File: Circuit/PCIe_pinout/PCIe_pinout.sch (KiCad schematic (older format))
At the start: 3 parts

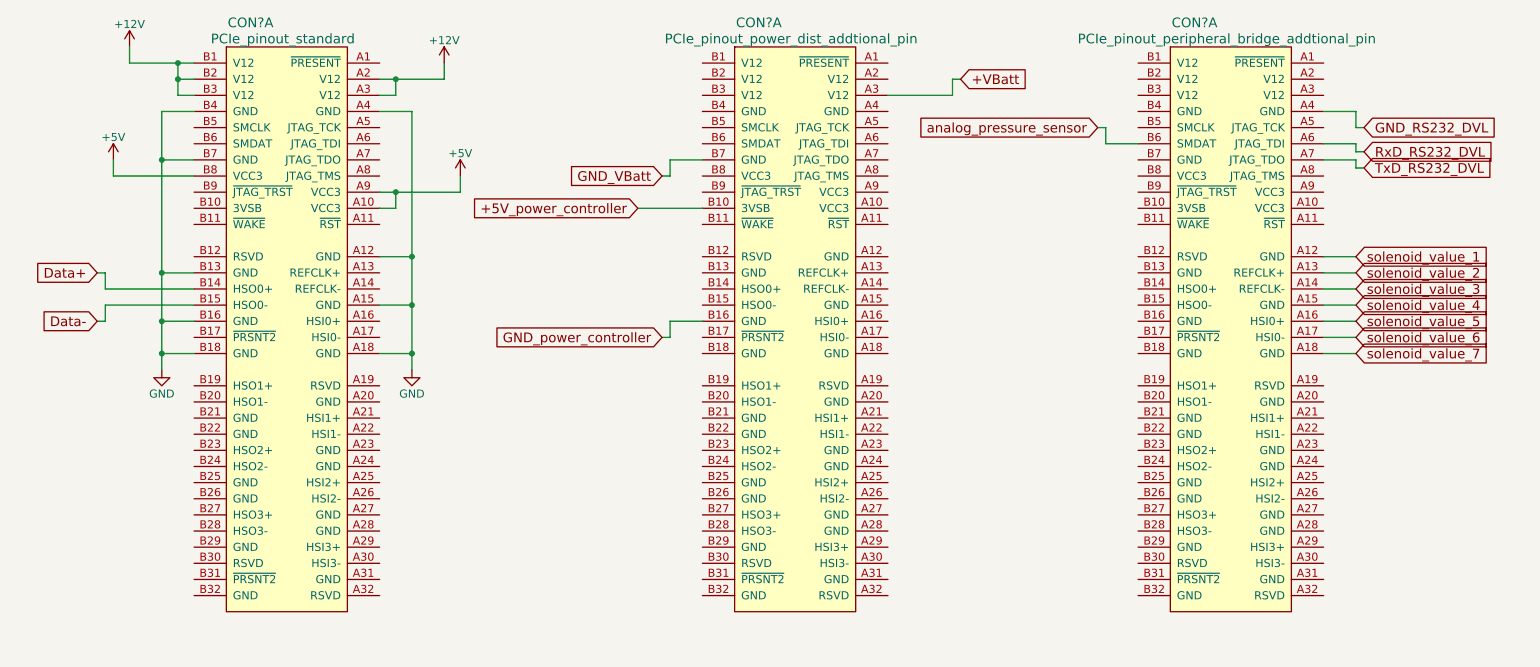
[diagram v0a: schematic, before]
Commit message: add addtional description
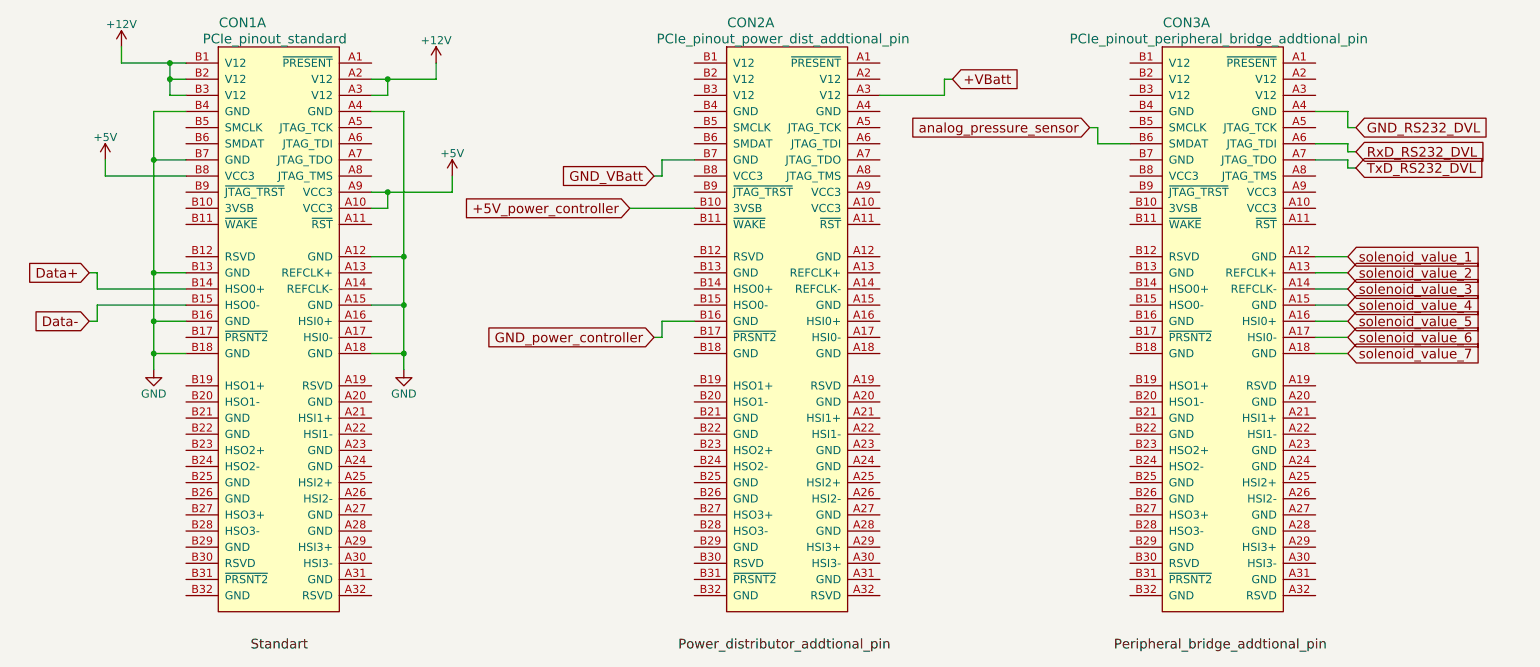
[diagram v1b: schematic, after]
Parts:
- gave numbers to parts that had none: 3
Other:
- moved on the sheet: CON1A, CON2A, CON3A

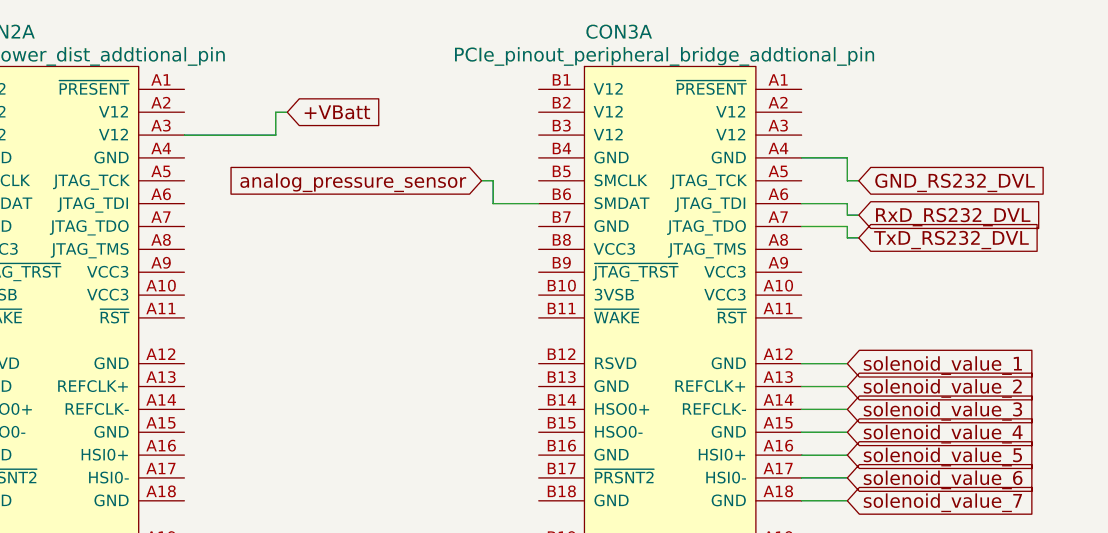
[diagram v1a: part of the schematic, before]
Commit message: added DSP_reset pins to PCIe_pinout
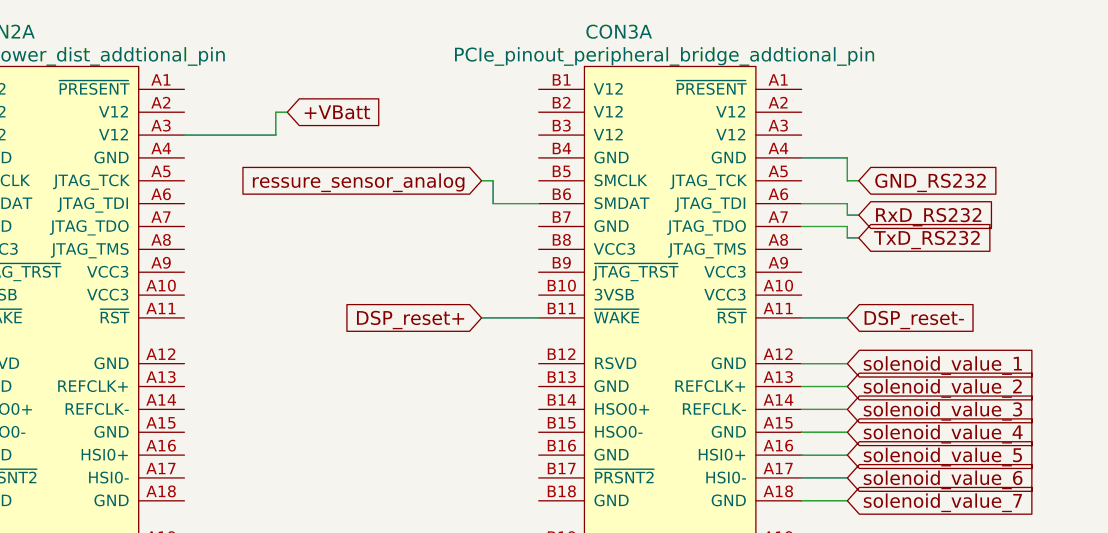
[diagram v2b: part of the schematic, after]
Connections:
- net DSP_reset-: now reaches CON3.A11 (~RST)
- net DSP_reset+: now reaches CON3.B11 (~WAKE)
- net GND_RS232_DVL renamed GND_RS232
- net RxD_RS232_DVL renamed RxD_RS232
- net TxD_RS232_DVL renamed TxD_RS232
- net analog_pressure_sensor renamed ressure_sensor_analog
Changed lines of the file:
@@
 LIBS:valves
 LIBS:zeabus
-LIBS:PCIe_pinout-cache
 EELAYER 25 0
 EELAYER END
@@
 $EndComp
 Text GLabel 7850 2500 0    60   Input ~ 0
-analog_pressure_sensor
+ressure_sensor_analog
 Wire Wire Line
 	7850 2500 7900 2500
@@
 	7900 2600 8100 2600
 Text GLabel 9500 2750 2    60   Input ~ 0
-TxD_RS232_DVL
+TxD_RS232
 Text GLabel 9500 2650 2    60   Input ~ 0
-RxD_RS232_DVL
+RxD_RS232
 Wire Wire Line
 	9250 2600 9450 2600
 Text GLabel 9500 2500 2    60   Input ~ 0
-GND_RS232_DVL
+GND_RS232
 Wire Wire Line
 	9450 2600 9450 2650
@@
 Text Label 8000 5750 0    60   ~ 0
 Peripheral_bridge_addtional_pin
+Text GLabel 7850 3100 0    60   Input ~ 0
+DSP_reset+
+Wire Wire Line
+	7850 3100 8100 3100
+Text GLabel 9450 3100 2    60   Input ~ 0
+DSP_reset-
+Wire Wire Line
+	9450 3100 9250 3100
 $EndSCHEMATC

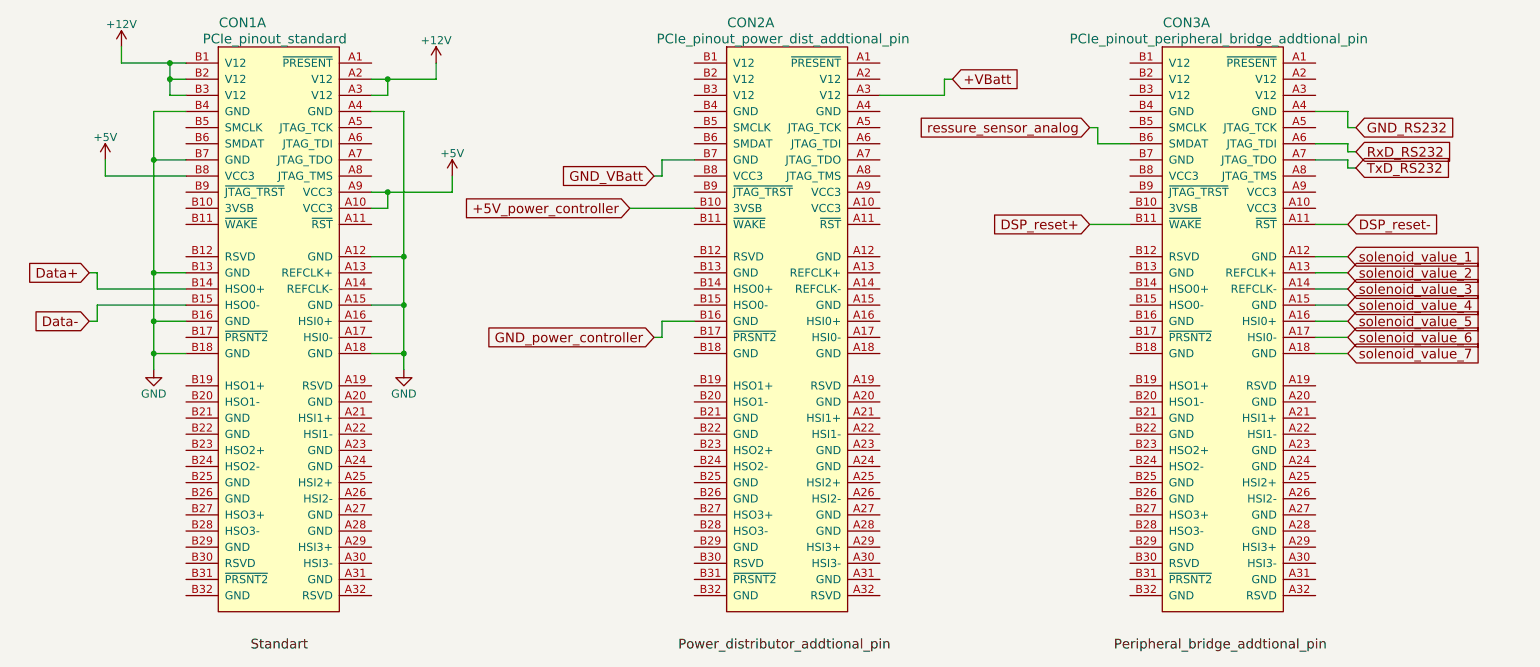
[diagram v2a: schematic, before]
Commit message: added planner_sw to PCIe_pinout
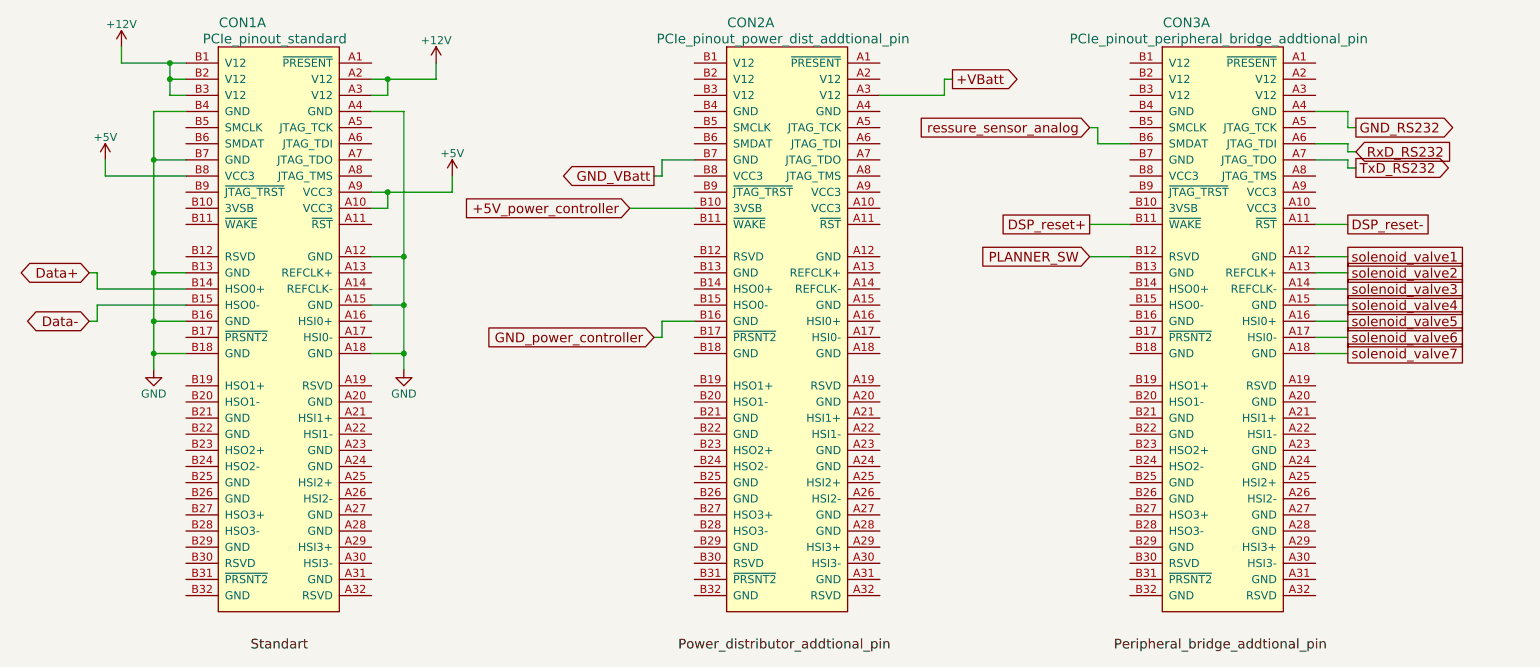
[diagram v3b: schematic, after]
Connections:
- net PLANNER_SW: now reaches CON3.B12 (RSVD)
- net solenoid_value_1 renamed solenoid_valve1
- net solenoid_value_2 renamed solenoid_valve2
- net solenoid_value_3 renamed solenoid_valve3
- net solenoid_value_4 renamed solenoid_valve4
- net solenoid_value_5 renamed solenoid_valve5
- net solenoid_value_6 renamed solenoid_valve6
- net solenoid_value_7 renamed solenoid_valve7
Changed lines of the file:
@@
 LIBS:valves
 LIBS:zeabus
+LIBS:PCIe_pinout-cache
 EELAYER 25 0
 EELAYER END
@@
 	1    0    0    -1
 $EndComp
-Text GLabel 1650 3400 0    60   Input ~ 0
+Text GLabel 1650 3400 0    60   BiDi ~ 0
 Data+
-Text GLabel 1650 3700 0    60   Input ~ 0
+Text GLabel 1650 3700 0    60   BiDi ~ 0
 Data-
 $Comp
@@
 Wire Wire Line
 	1700 3600 2250 3600
-Text GLabel 7000 2200 2    60   Input ~ 0
+Text GLabel 7000 2200 2    60   Output ~ 0
 +VBatt
 Wire Wire Line
 	6950 2200 7000 2200
-Text GLabel 5150 2800 0    60   Input ~ 0
+Text GLabel 5150 2800 0    60   Output ~ 0
 GND_VBatt
 Wire Wire Line
@@
 Wire Wire Line
 	7900 2600 8100 2600
-Text GLabel 9500 2750 2    60   Input ~ 0
+Text GLabel 9500 2750 2    60   Output ~ 0
 TxD_RS232
 Text GLabel 9500 2650 2    60   Input ~ 0
@@
 Wire Wire Line
 	9250 2600 9450 2600
-Text GLabel 9500 2500 2    60   Input ~ 0
+Text GLabel 9500 2500 2    60   Output ~ 0
 GND_RS232
 Wire Wire Line
@@
 Wire Wire Line
 	9450 2400 9250 2400
-Text GLabel 9450 3300 2    60   Input ~ 0
-solenoid_value_1
+Text GLabel 9450 3300 2    60   UnSpc ~ 0
+solenoid_valve1
 Wire Wire Line
 	9250 3300 9450 3300
-Text GLabel 9450 3400 2    60   Input ~ 0
-solenoid_value_2
-Text GLabel 9450 3500 2    60   Input ~ 0
-solenoid_value_3
-Text GLabel 9450 3600 2    60   Input ~ 0
-solenoid_value_4
-Text GLabel 9450 3700 2    60   Input ~ 0
-solenoid_value_5
-Text GLabel 9450 3800 2    60   Input ~ 0
-solenoid_value_6
-Text GLabel 9450 3900 2    60   Input ~ 0
-solenoid_value_7
 Wire Wire Line
 	9450 3900 9250 3900
@@
 Text Label 8000 5750 0    60   ~ 0
 Peripheral_bridge_addtional_pin
-Text GLabel 7850 3100 0    60   Input ~ 0
+Text GLabel 7850 3100 0    60   UnSpc ~ 0
 DSP_reset+
 Wire Wire Line
 	7850 3100 8100 3100
-Text GLabel 9450 3100 2    60   Input ~ 0
+Text GLabel 9450 3100 2    60   UnSpc ~ 0
 DSP_reset-
 Wire Wire Line
 	9450 3100 9250 3100
+Text GLabel 7850 3300 0    60   Input ~ 0
+PLANNER_SW
+Wire Wire Line
+	8100 3300 7850 3300
+Text GLabel 9450 3400 2    60   UnSpc ~ 0
+solenoid_valve2
+Text GLabel 9450 3500 2    60   UnSpc ~ 0
+solenoid_valve3
+Text GLabel 9450 3600 2    60   UnSpc ~ 0
+solenoid_valve4
+Text GLabel 9450 3700 2    60   UnSpc ~ 0
+solenoid_valve5
+Text GLabel 9450 3800 2    60   UnSpc ~ 0
+solenoid_valve6
+Text GLabel 9450 3900 2    60   UnSpc ~ 0
+solenoid_valve7
 $EndSCHEMATC

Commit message: added DSP_reset, planner_sw, kill_sw_pwr, sys_sw_pwr to backplane
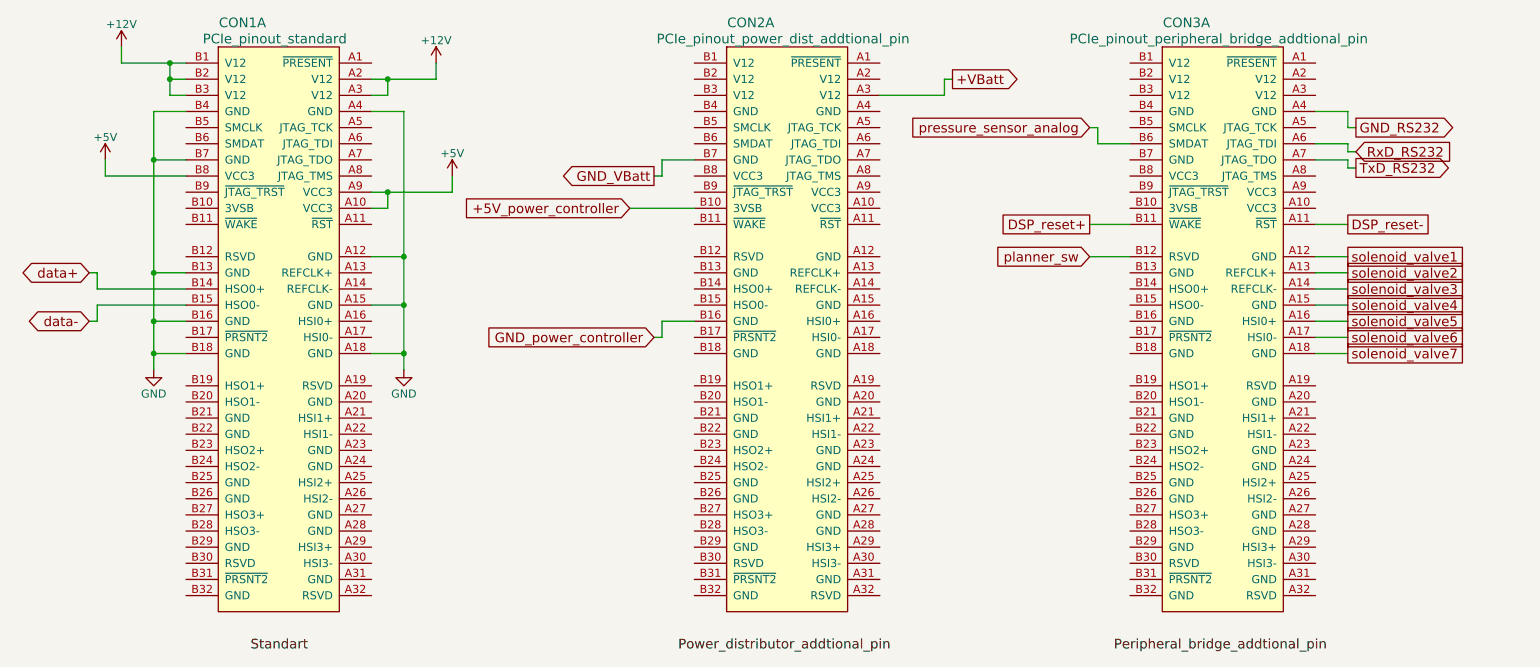
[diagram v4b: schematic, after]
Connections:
- net Data+ renamed data+
- net Data- renamed data-
- net PLANNER_SW renamed planner_sw
- net ressure_sensor_analog renamed pressure_sensor_analog
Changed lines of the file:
@@
 $EndComp
 Text GLabel 1650 3400 0    60   BiDi ~ 0
-Data+
+data+
 Text GLabel 1650 3700 0    60   BiDi ~ 0
-Data-
+data-
 $Comp
 L Conn-PCIE-x16 CON2
@@
 $EndComp
 Text GLabel 7850 2500 0    60   Input ~ 0
-ressure_sensor_analog
+pressure_sensor_analog
 Wire Wire Line
 	7850 2500 7900 2500
@@
 	9450 3100 9250 3100
 Text GLabel 7850 3300 0    60   Input ~ 0
-PLANNER_SW
+planner_sw
 Wire Wire Line
 	8100 3300 7850 3300

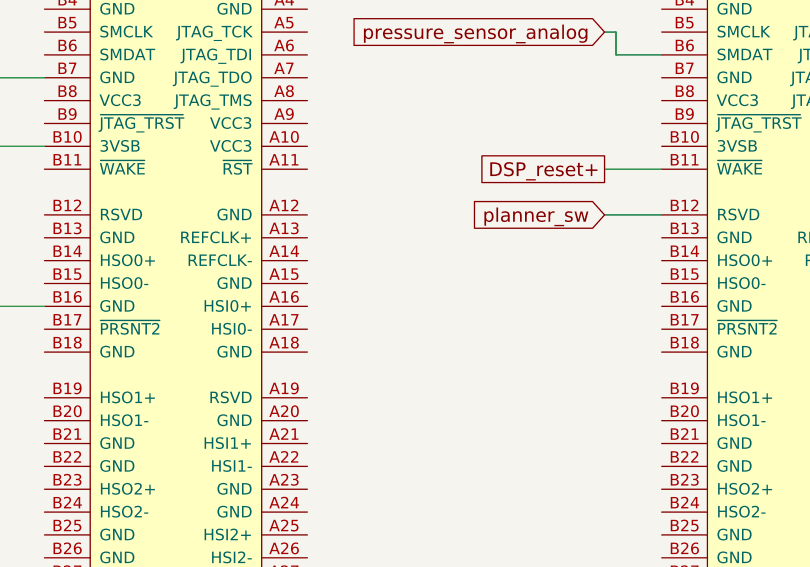
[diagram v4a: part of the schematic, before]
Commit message: added KILL_SW and SYS_SW to power_distributor pinout
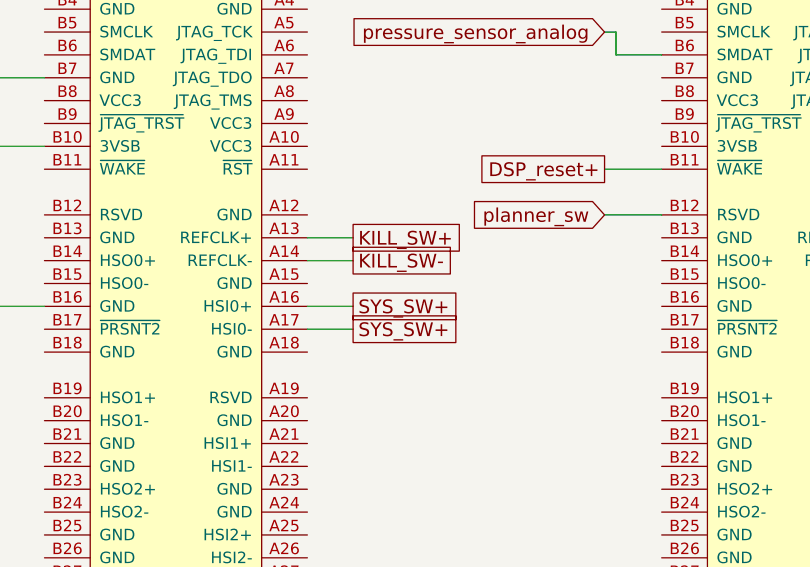
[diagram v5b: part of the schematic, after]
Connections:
- net KILL_SW+: now reaches CON2.A13 (REFCLK+)
- net KILL_SW-: now reaches CON2.A14 (REFCLK-)
- net SYS_SW+: now reaches CON2.A16 (HSI0+)
- net SYS_SW+: now also CON2.A17 (HSI0-)
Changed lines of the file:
@@
 Text GLabel 9450 3900 2    60   UnSpc ~ 0
 solenoid_valve7
+Text GLabel 6750 3400 2    60   UnSpc ~ 0
+KILL_SW+
+Text GLabel 6750 3700 2    60   UnSpc ~ 0
+SYS_SW+
+Text GLabel 6750 3500 2    60   UnSpc ~ 0
+KILL_SW-
+Wire Wire Line
+	6550 3400 6750 3400
+Wire Wire Line
+	6750 3500 6550 3500
+Text GLabel 6750 3800 2    60   UnSpc ~ 0
+SYS_SW+
+Wire Wire Line
+	6750 3700 6550 3700
+Wire Wire Line
+	6550 3800 6750 3800
 $EndSCHEMATC
